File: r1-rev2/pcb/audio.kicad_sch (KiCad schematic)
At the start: 26 parts, among them J3 HP_3.5mm, J4 LO_3.5mm, Q4 AO3401A, Q5 AO3401A, U15 TPAZ1143-04F, U16 TPAZ1143-04F, U3 TLV320AIC3104

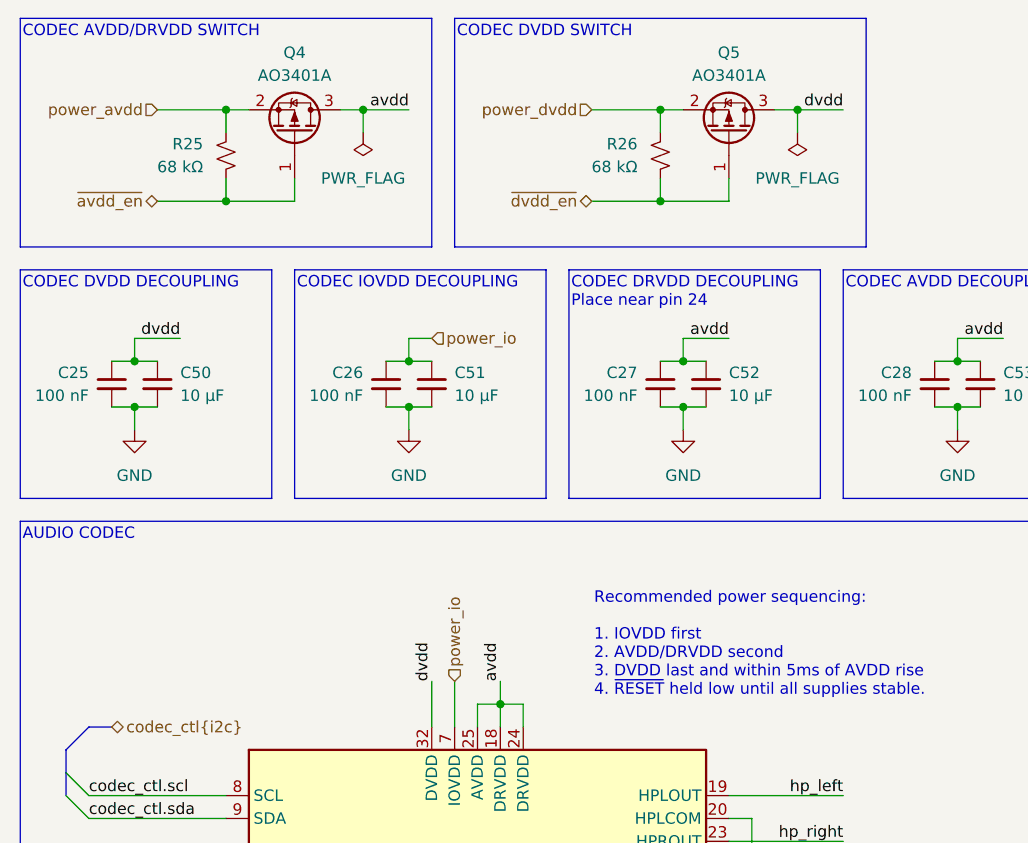
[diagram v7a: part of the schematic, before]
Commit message: R1-Rev2: use LDO enable pin to control codec AVDD supply
Now that the codec has a dedicated power supply for AVDD,
the LDO's enable pin can be used for power sequencing.
This eliminates a resistor and PMOS.
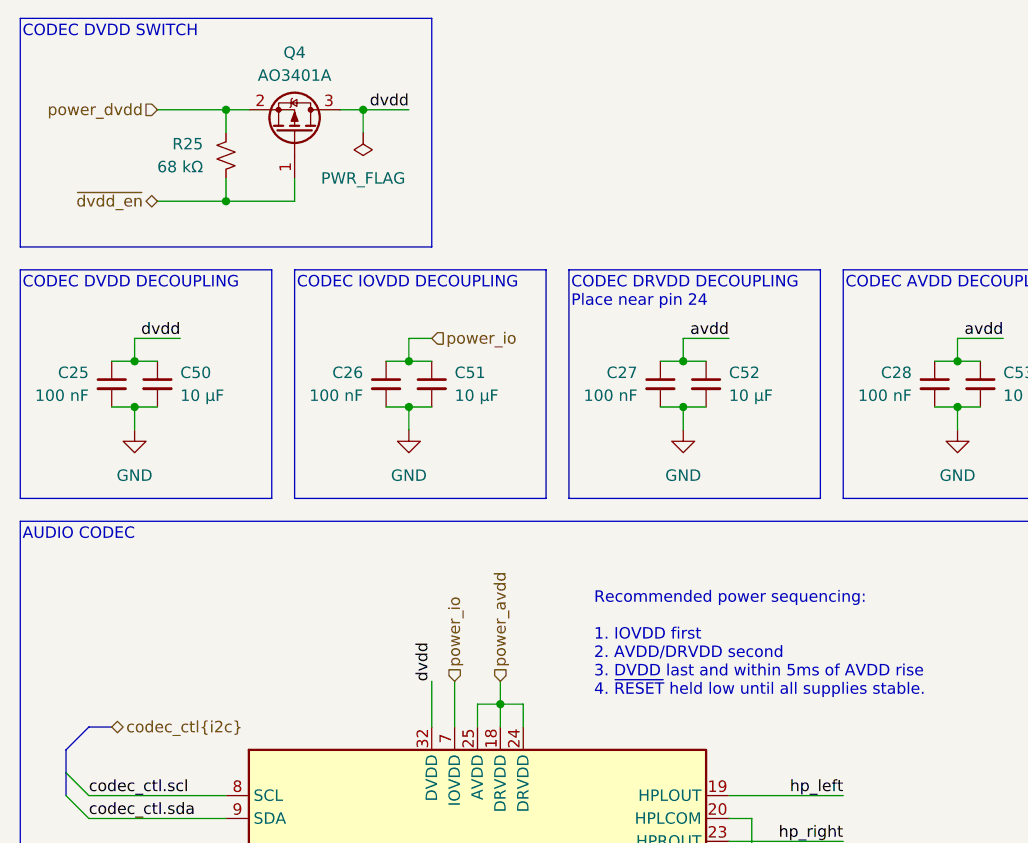
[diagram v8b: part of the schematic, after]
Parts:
- removed Q4: AO3401A, Package_TO_SOT_SMD:SOT-23, symbol Device:Q_PMOS_GSD
- removed R25: 68 kΩ, Resistor_SMD:R_0402_1005Metric, symbol Device:R_Small_US
- renumbered Q5 to Q4, R26 to R25
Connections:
- net avdd: no longer U3.18 (DRVDD), U3.24 (DRVDD), U3.25 (AVDD)
- net power_avdd: now also U3.18 (DRVDD), U3.24 (DRVDD), U3.25 (AVDD)
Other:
- note removed: "CODEC AVDD/DRVDD SWITCH"
- moved on the sheet: Q4, R25
